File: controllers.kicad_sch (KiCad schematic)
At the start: 6 parts, among them SW3 SW_DPST_x2, SW4 SW_DPST_x2

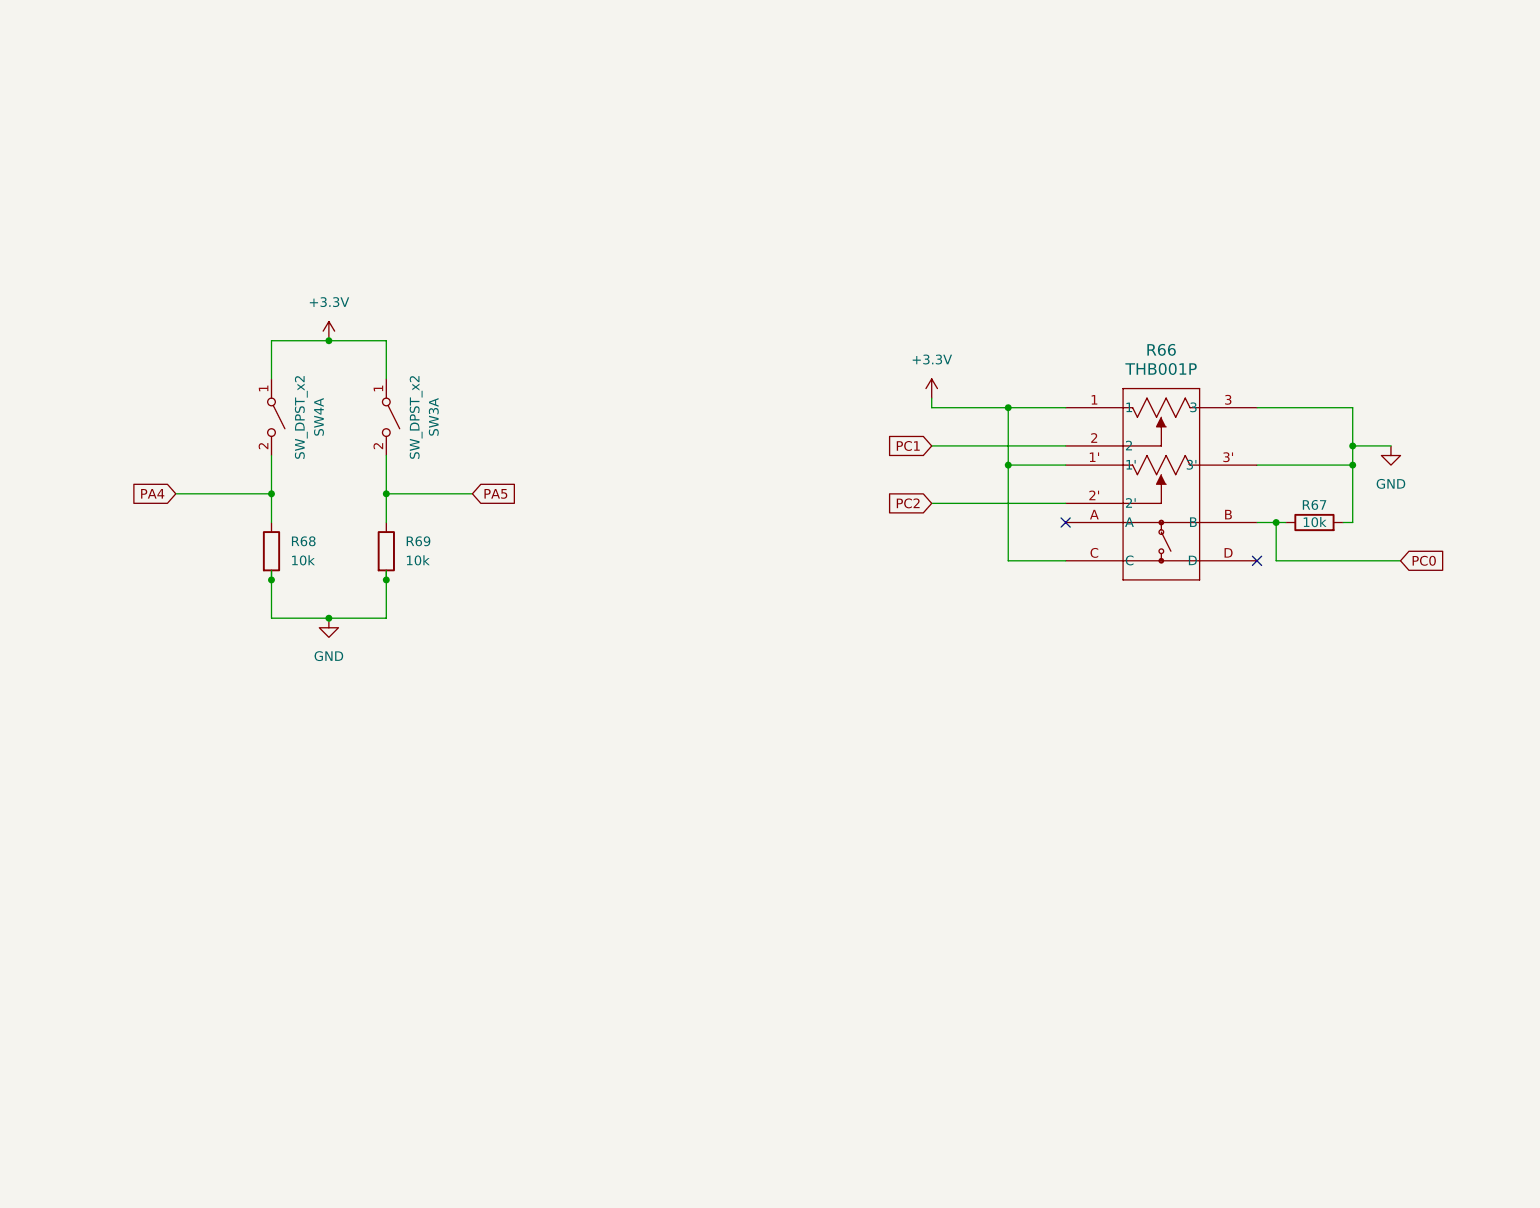
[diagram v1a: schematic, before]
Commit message: updated footprints
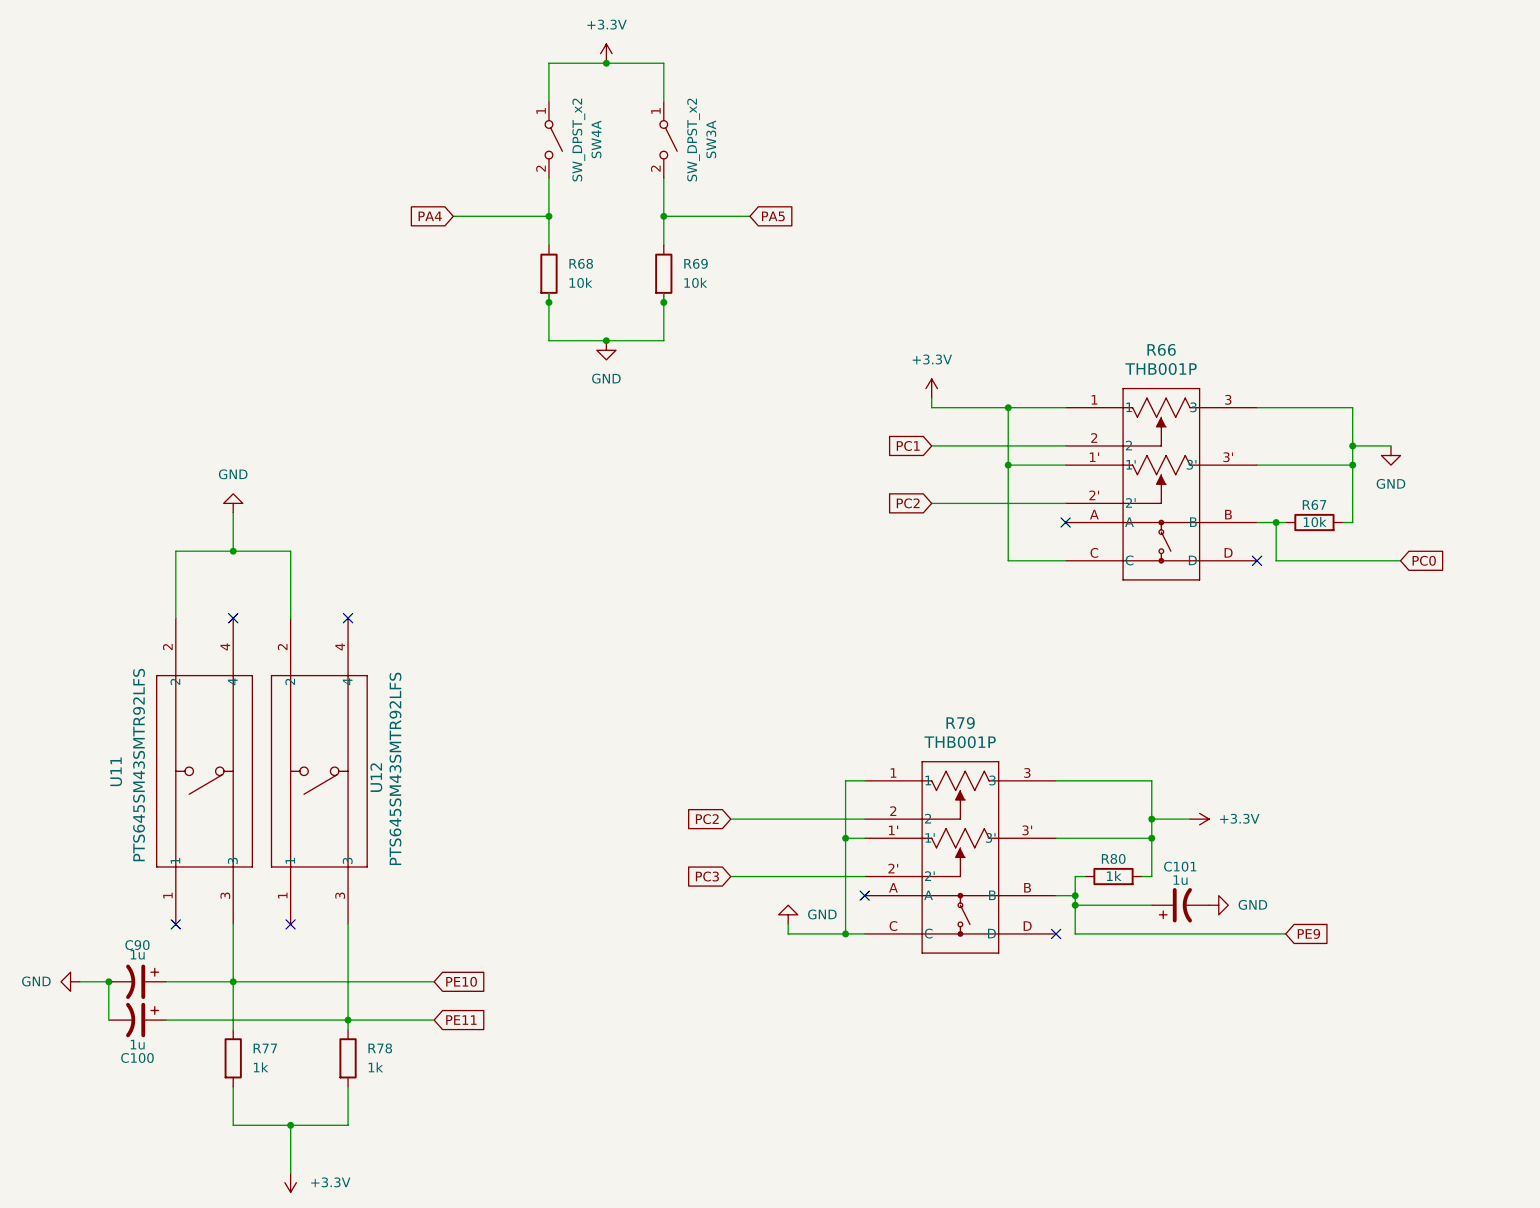
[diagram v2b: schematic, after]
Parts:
- added C100, C101, C90: 1u, symbol Device:C_Polarized_US
- added R77, R78, R80: 1k, Resistor_SMD:R_0805_2012Metric, symbol Device:R
- added R79: THB001P, joystick:THB001P_CNK, symbol THB001P:THB001P
- added U11, U12: PTS645SM43SMTR92LFS, PTS645SM43SMTR92-LFS:SWITCH_43SMTR92LFS, symbol PTS645SM43SMTR92-LFS:PTS645SM43SMTR92LFS
- R66: footprint THB001P_CNK -> joystick:THB001P_CNK
- R67, R68, R69: footprint (none) -> Resistor_SMD:R_0805_2012Metric
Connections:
- net +3.3V: now also R77.2, R78.2, R79.3, R79.3', R80.2
- net GND: now also C100.2, C101.2, C90.2, R79.1, R79.1', R79.C, U11.2, U12.2
- net PC2: now also R79.2
- new net PC3: R79.2'
- new net PE10: C90.1, R77.1, U11.3
- new net PE11: C100.1, R78.1, U12.3
- new net PE9: C101.1, R79.B, R80.1
- no-connect marks 2 -> 8
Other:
- moved on the sheet: R68, R69, SW3A, SW4A

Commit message: Fixed schematic comments
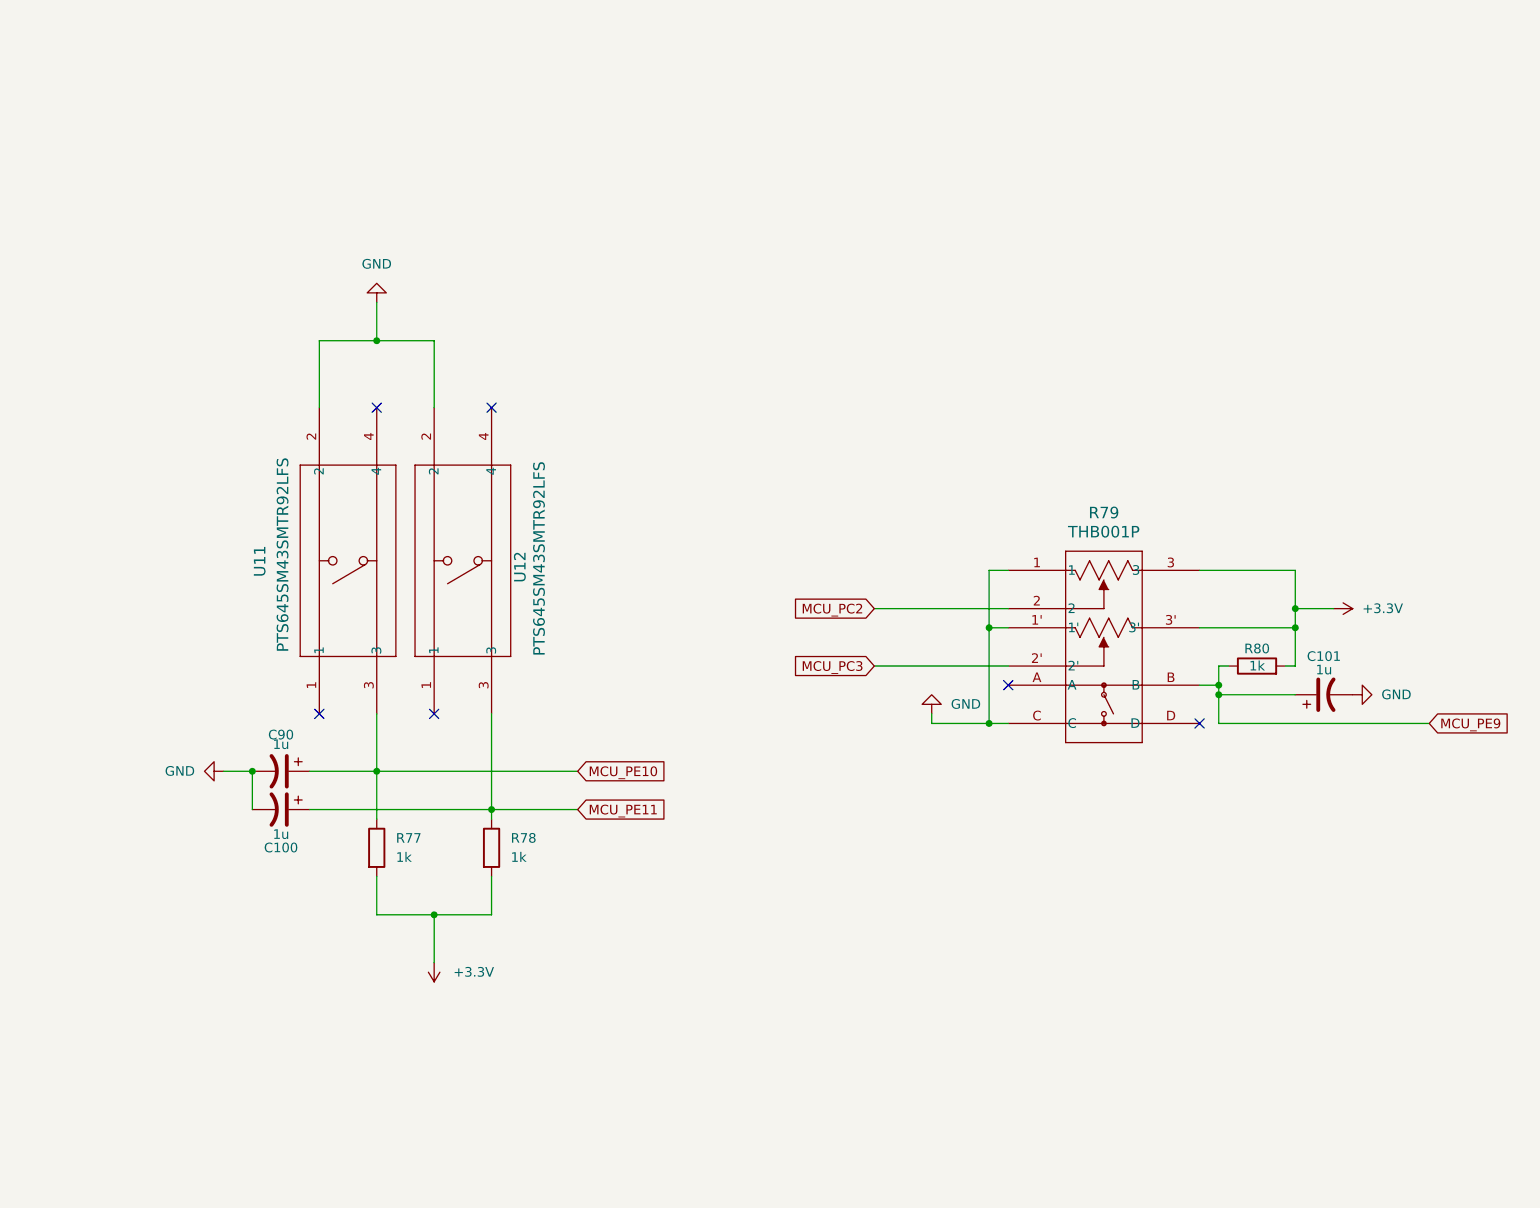
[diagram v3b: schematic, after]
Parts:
- removed R66: THB001P, joystick:THB001P_CNK, symbol THB001P:THB001P
- removed R67, R68, R69: 10k, Resistor_SMD:R_0805_2012Metric, symbol Device:R
- removed SW3, SW4: SW_DPST_x2, symbol Switch:SW_DPST_x2
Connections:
- net PC2 renamed MCU_PC2
- net PC3 renamed MCU_PC3
- net PE10 renamed MCU_PE10
- net PE11 renamed MCU_PE11
- net PE9 renamed MCU_PE9
- no-connect marks 8 -> 6
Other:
- moved on the sheet: C100, C101, C90, R77, R78, R79, R80, U11, U12
